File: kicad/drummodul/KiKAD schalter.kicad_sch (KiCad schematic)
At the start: 27 parts, among them J1 Conn_02x08_Odd_Even, J2 Conn_01x02_Pin, J3 Conn_01x02_Pin, Q1 Q_NPN_BCE, Q2 Q_NPN_ECB

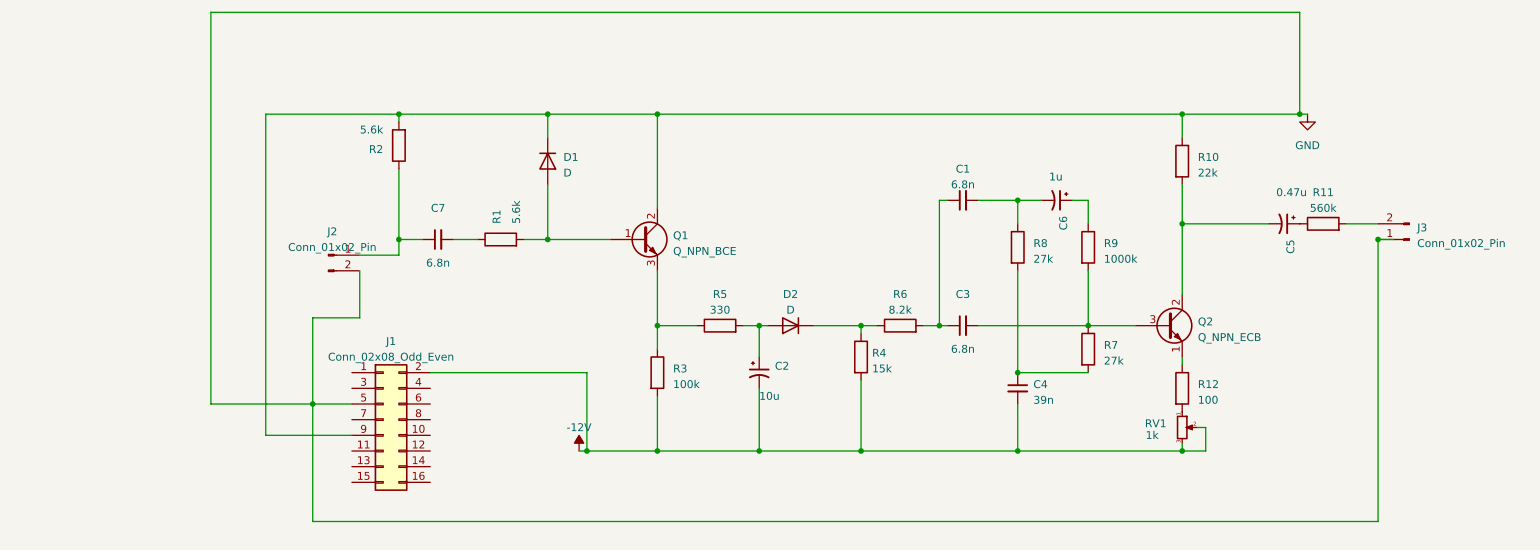
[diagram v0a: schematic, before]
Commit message: drummodul schaltplan angepasst
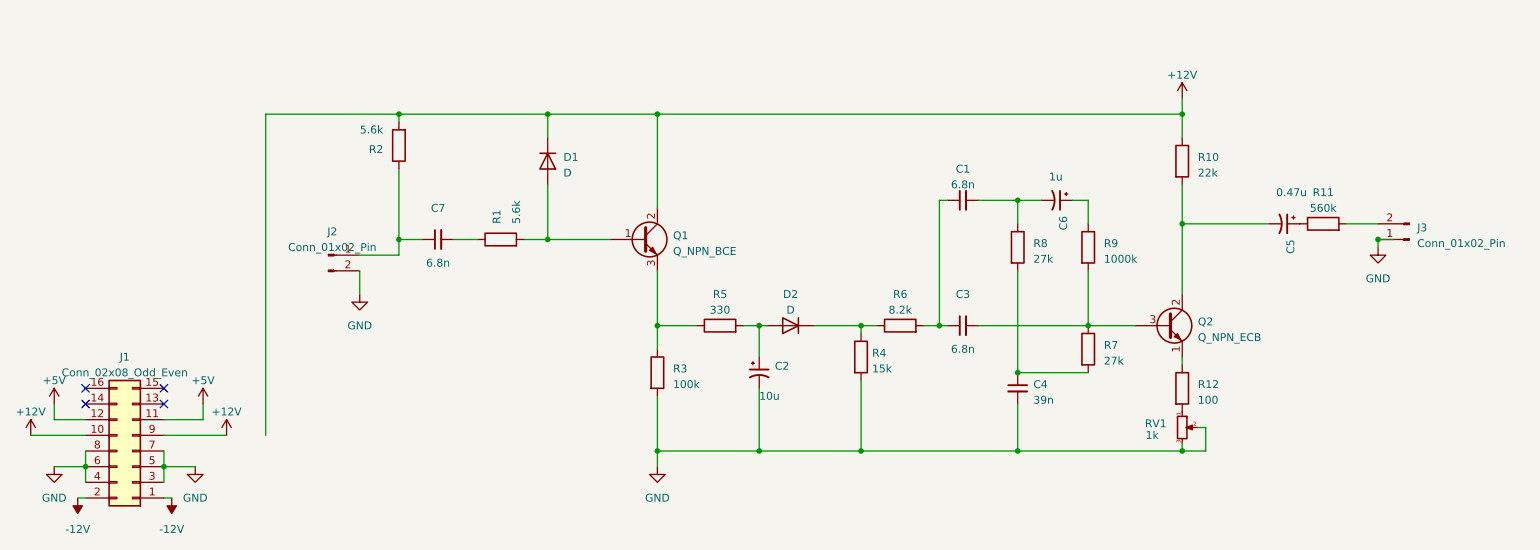
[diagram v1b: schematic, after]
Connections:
- net -12V: now also J1.1 (Pin_1); no longer C2.2, C4.2, R3.2, R4.2, RV1.2, RV1.3
- net GND: now also C2.2, C4.2, J1.3 (Pin_3), J1.4 (Pin_4), J1.6 (Pin_6), J1.7 (Pin_7), J1.8 (Pin_8), R3.2, R4.2, RV1.2, RV1.3; no longer D1.1 (K), J1.9 (Pin_9), Q1.2 (C), R10.1, R2.2
- net +12V: now reaches J1.10 (Pin_10)
- net +12V: now also D1.1 (K), J1.9 (Pin_9), Q1.2 (C), R10.1, R2.2
- net +5V: now reaches J1.11 (Pin_11)
- net +5V: now also J1.12 (Pin_12)
- no-connect marks 0 -> 4
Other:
- moved on the sheet: J1
